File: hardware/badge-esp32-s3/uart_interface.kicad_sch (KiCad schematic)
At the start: 4 parts, among them U1 ESP32-S3-WROOM-1(N16R8)

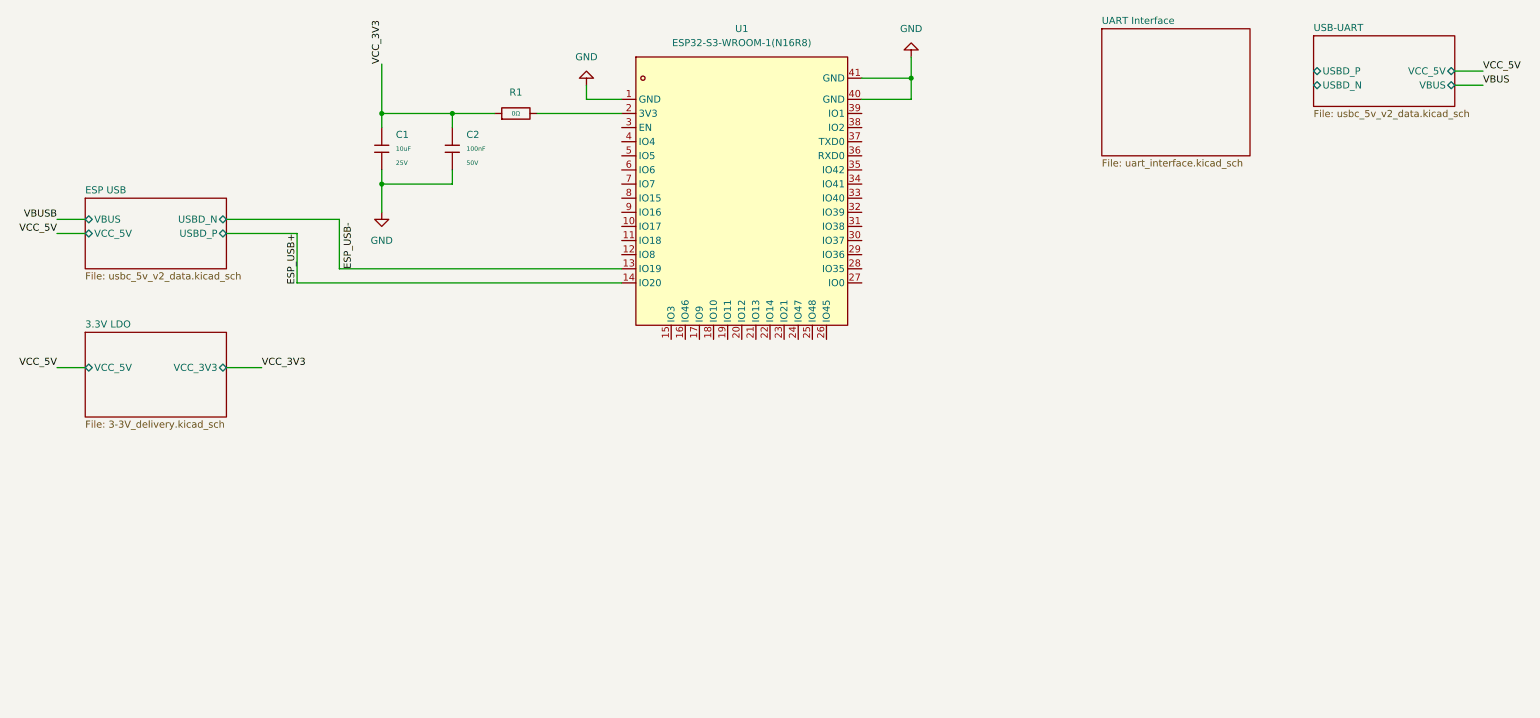
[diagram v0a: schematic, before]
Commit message: Finish linear regulator, start uart interface
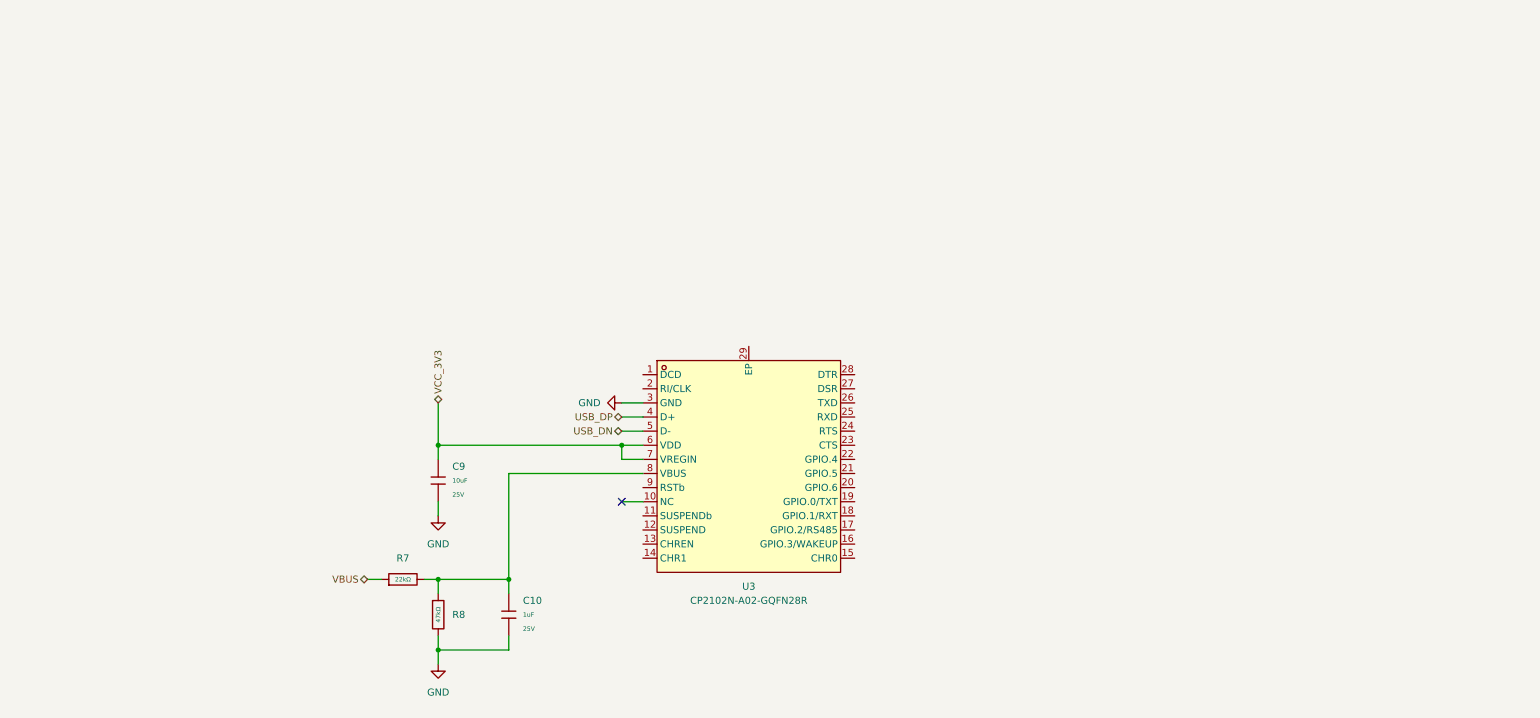
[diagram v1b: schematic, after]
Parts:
- removed C1: 10uF, PCM_JLCPCB:C_0603, symbol PCM_JLCPCB-Capacitors:0603,10uF,(2)
- removed C2: 100nF, PCM_JLCPCB:C_0603, symbol PCM_JLCPCB-Capacitors:0603,100nF
- removed R1: 0Ω, PCM_JLCPCB:R_0402, symbol PCM_JLCPCB-Resistors:0402,0Ω
- removed U1: ESP32-S3-WROOM-1(N16R8), lcsc-lib:WIRELM-SMD_ESP32-S3-WROOM-1, symbol lcsc-lib:ESP32-S3-WROOM-1(N16R8)
- added C10: 1uF, PCM_JLCPCB:C_0402, symbol PCM_JLCPCB-Capacitors:0402,1uF
- added C9: 10uF, PCM_JLCPCB:C_0603, symbol PCM_JLCPCB-Capacitors:0603,10uF,(2)
- added R7: 22kΩ, PCM_JLCPCB:R_0402, symbol PCM_JLCPCB-Resistors:0402,22kΩ
- added R8: 47kΩ, PCM_JLCPCB:R_0402, symbol PCM_JLCPCB-Resistors:0402,47kΩ
- added U3: CP2102N-A02-GQFN28R, lcsc-lib:QFN-28_L5.0-W5.0-P0.50-TL-EP3.3, symbol lcsc-lib:CP2102N-A02-GQFN28R
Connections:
- net GND: now also C10.2, C9.2, R8.2, U3.3 (GND)
- net VBUS: now also R7.1
- net VCC_3V3: now also C9.1, U3.6 (VDD), U3.7 (VREGIN)
- new net: C10.1, R7.2, R8.1, U3.8 (VBUS)
- new net USB_DN: U3.5 (D-)
- new net USB_DP: U3.4 (D+)
- no-connect marks 0 -> 1
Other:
- removed sheet 3.3V LDO
- removed sheet ESP USB
- removed sheet UART Interface
- removed sheet USB-UART

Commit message: Finish USB-UART subcircuit
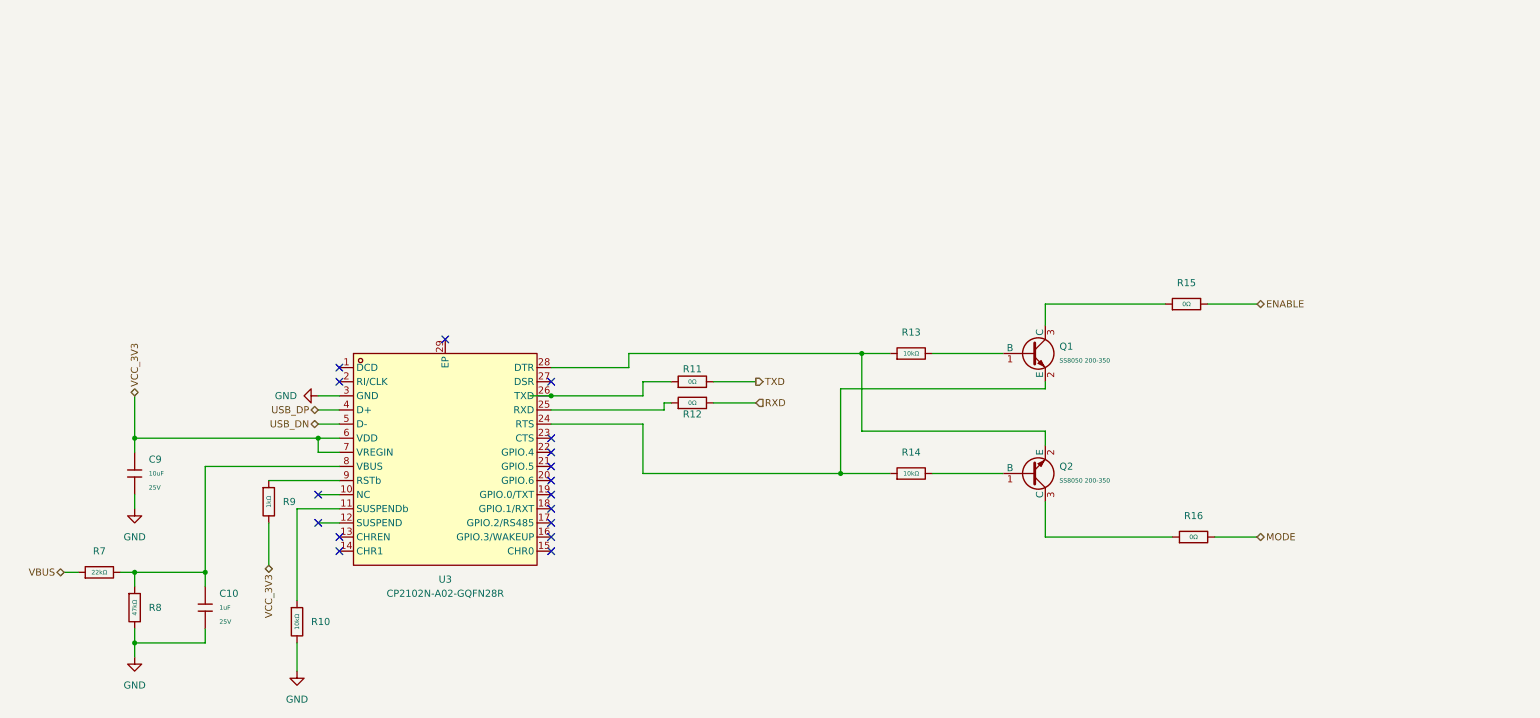
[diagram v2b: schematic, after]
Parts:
- added Q1, Q2: SS8050 200-350, PCM_JLCPCB:Q_SOT-23, symbol PCM_JLCPCB-Transistors:NPN,SS8050 200-350
- added R10, R13, R14: 10kΩ, PCM_JLCPCB:R_0402, symbol PCM_JLCPCB-Resistors:0402,10kΩ
- added R11, R12, R15, R16: 0Ω, PCM_JLCPCB:R_0402, symbol PCM_JLCPCB-Resistors:0402,0Ω
- added R9: 1kΩ, PCM_JLCPCB:R_0402, symbol PCM_JLCPCB-Resistors:0402,1kΩ
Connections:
- net GND: now also R10.2
- net VCC_3V3: now also R9.2
- net at U3.11 (SUSPENDb): now also R10.1
- net at U3.24 (RTS): now also Q1.2 (E), R14.1
- net at U3.25 (RXD): now also R12.1
- net at U3.26 (TXD): now also R11.1
- net at U3.28 (DTR): now also Q2.2 (E), R13.1
- net at U3.9 (RSTb): now also R9.1
- new net: Q1.3 (C), R15.1
- new net: Q2.1 (B), R14.2
- new net: Q2.3 (C), R16.1
- new net: Q1.1 (B), R13.2
- new net ENABLE: R15.2
- new net MODE: R16.2
- new net RXD: R12.2
- new net TXD: R11.2
- no-connect marks 1 -> 17
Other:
- moved on the sheet: C10, C9, R7, R8, U3

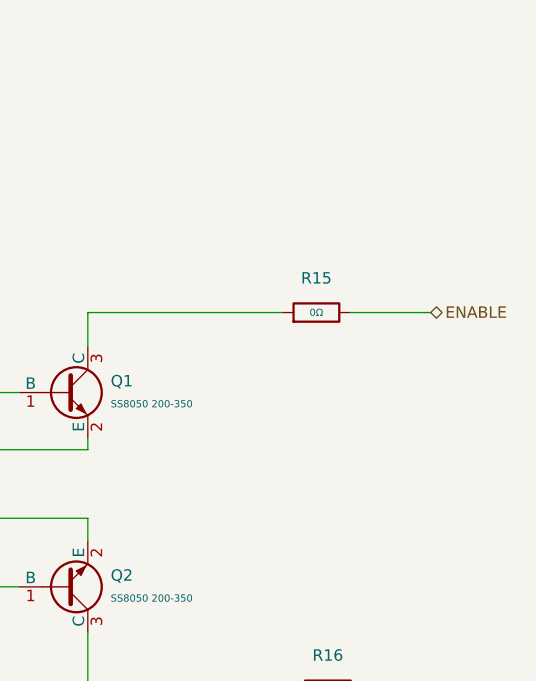
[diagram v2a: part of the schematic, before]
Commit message: Schematic on par with basic devkit
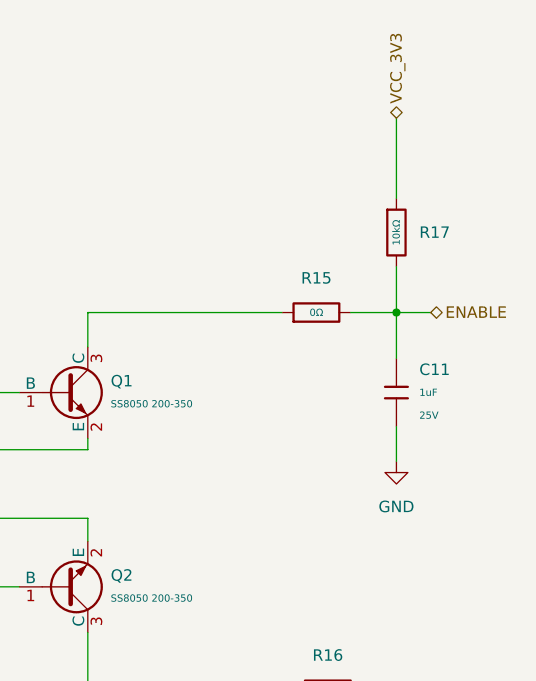
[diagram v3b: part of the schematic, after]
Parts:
- added C11: 1uF, PCM_JLCPCB:C_0402, symbol PCM_JLCPCB-Capacitors:0402,1uF
- added R17: 10kΩ, PCM_JLCPCB:R_0402, symbol PCM_JLCPCB-Resistors:0402,10kΩ
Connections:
- net ENABLE: now also C11.1, R17.2
- net GND: now also C11.2
- net VCC_3V3: now also R17.1

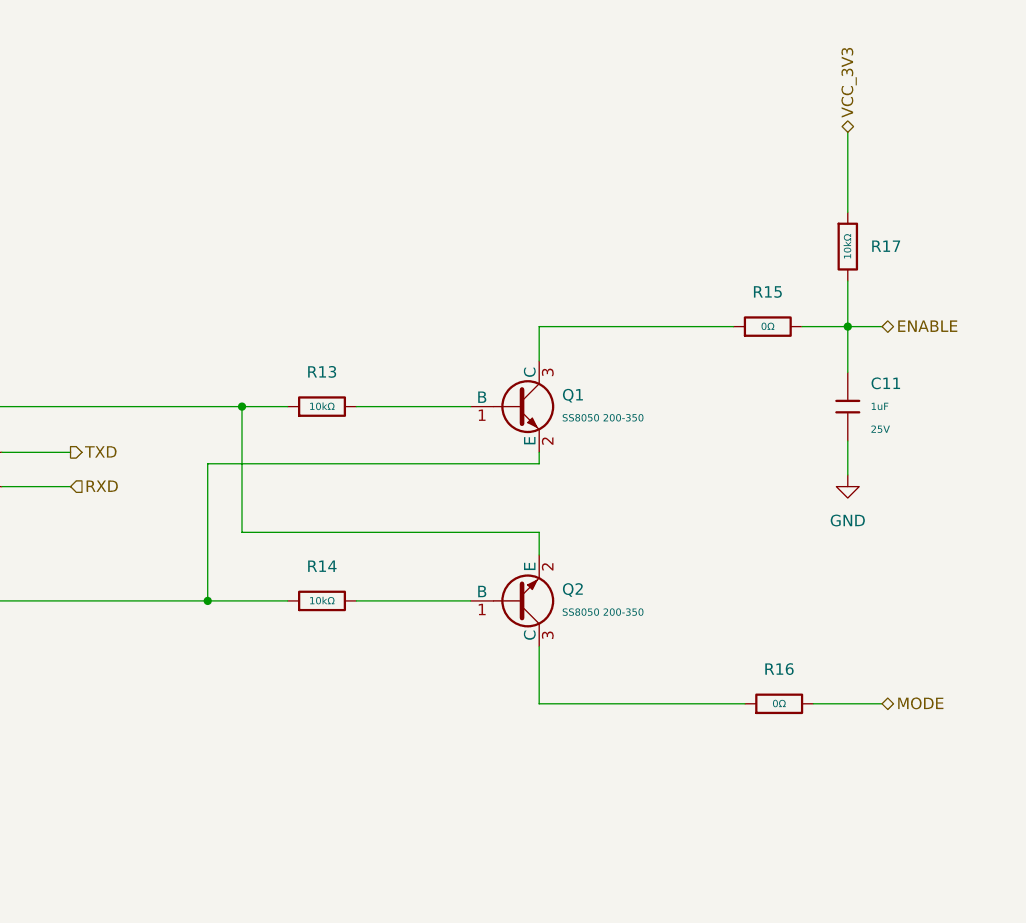
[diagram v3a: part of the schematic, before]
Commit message: add display block
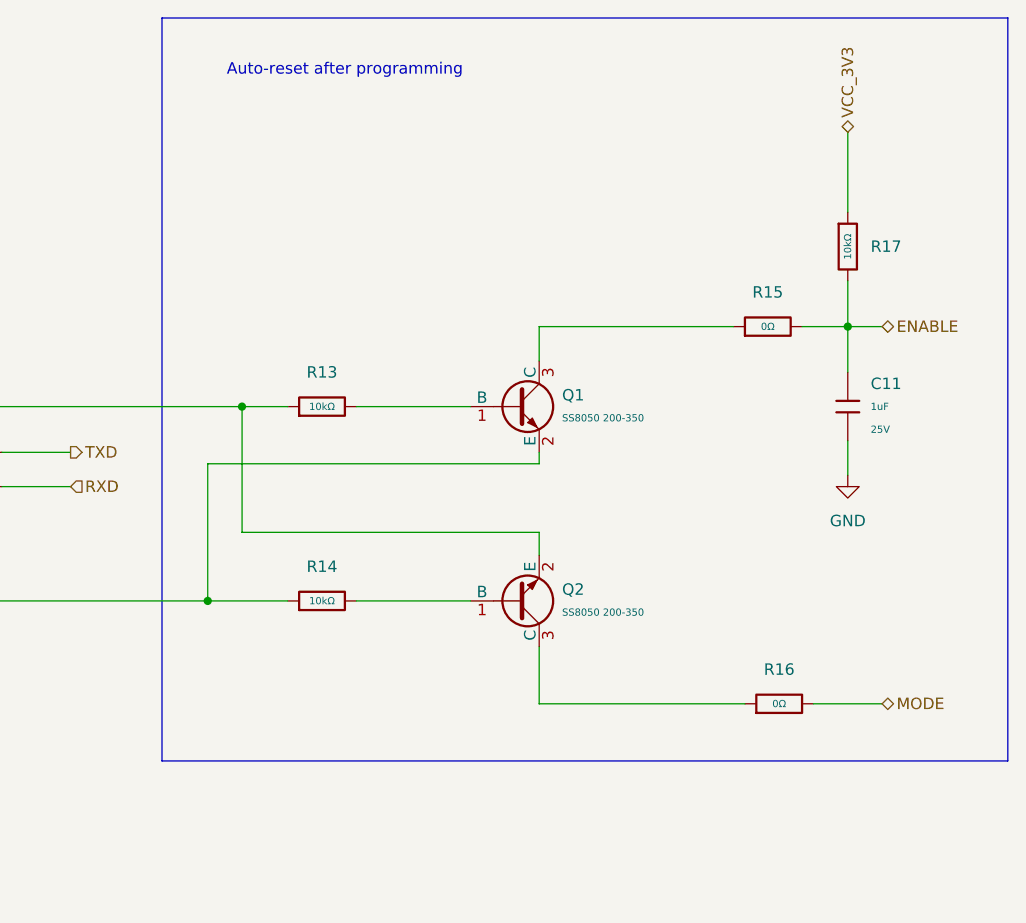
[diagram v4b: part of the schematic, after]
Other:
- note added: "Auto-reset after programming"
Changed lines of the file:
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@@
 	(generator_version "9.0")
 	(paper "A4")
+	(rectangle
+		(start 156.21 30.48)
+		(end 250.19 113.03)
+		(stroke
+			(width 0)
+			(type default)
+		)
+		(fill
+			(type none)
+		)
+	)
+	(text "Auto-reset after programming"
+		(exclude_from_sim yes)
+		(at 176.53 36.322 0)
+		(effects
+			(font
+				(size 1.27 1.27)
+			)
+		)
+	)
 	(junction
 		(at 34.29 113.03)
